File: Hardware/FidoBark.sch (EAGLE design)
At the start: 56 parts, among them Q1 MMBT2222A, T1 BPX81, U1 EDISON_CONNECTOR_FULLHEADER, U3 MCP73831, U4 TXB0108, U5 ADS1015, U6 PCA9306, U8 LSM9DS0

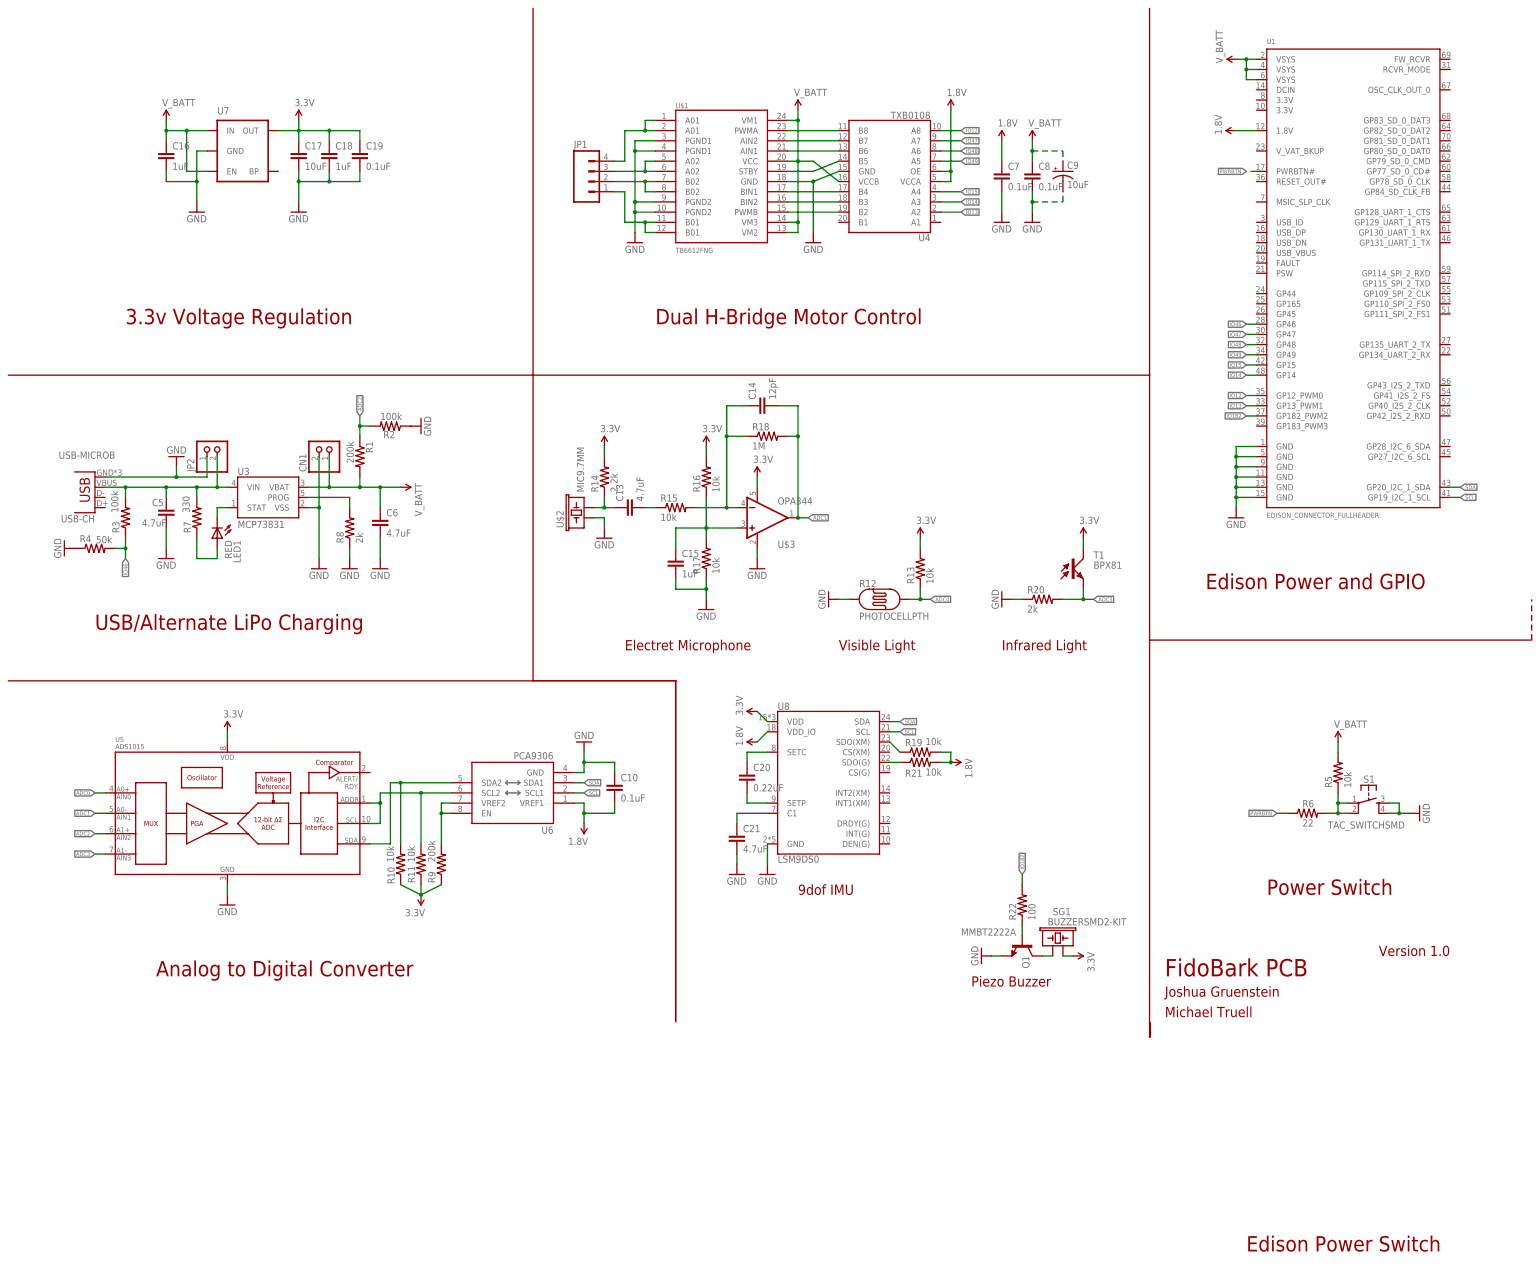
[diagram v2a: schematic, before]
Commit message: Cortex M4F based schematic start
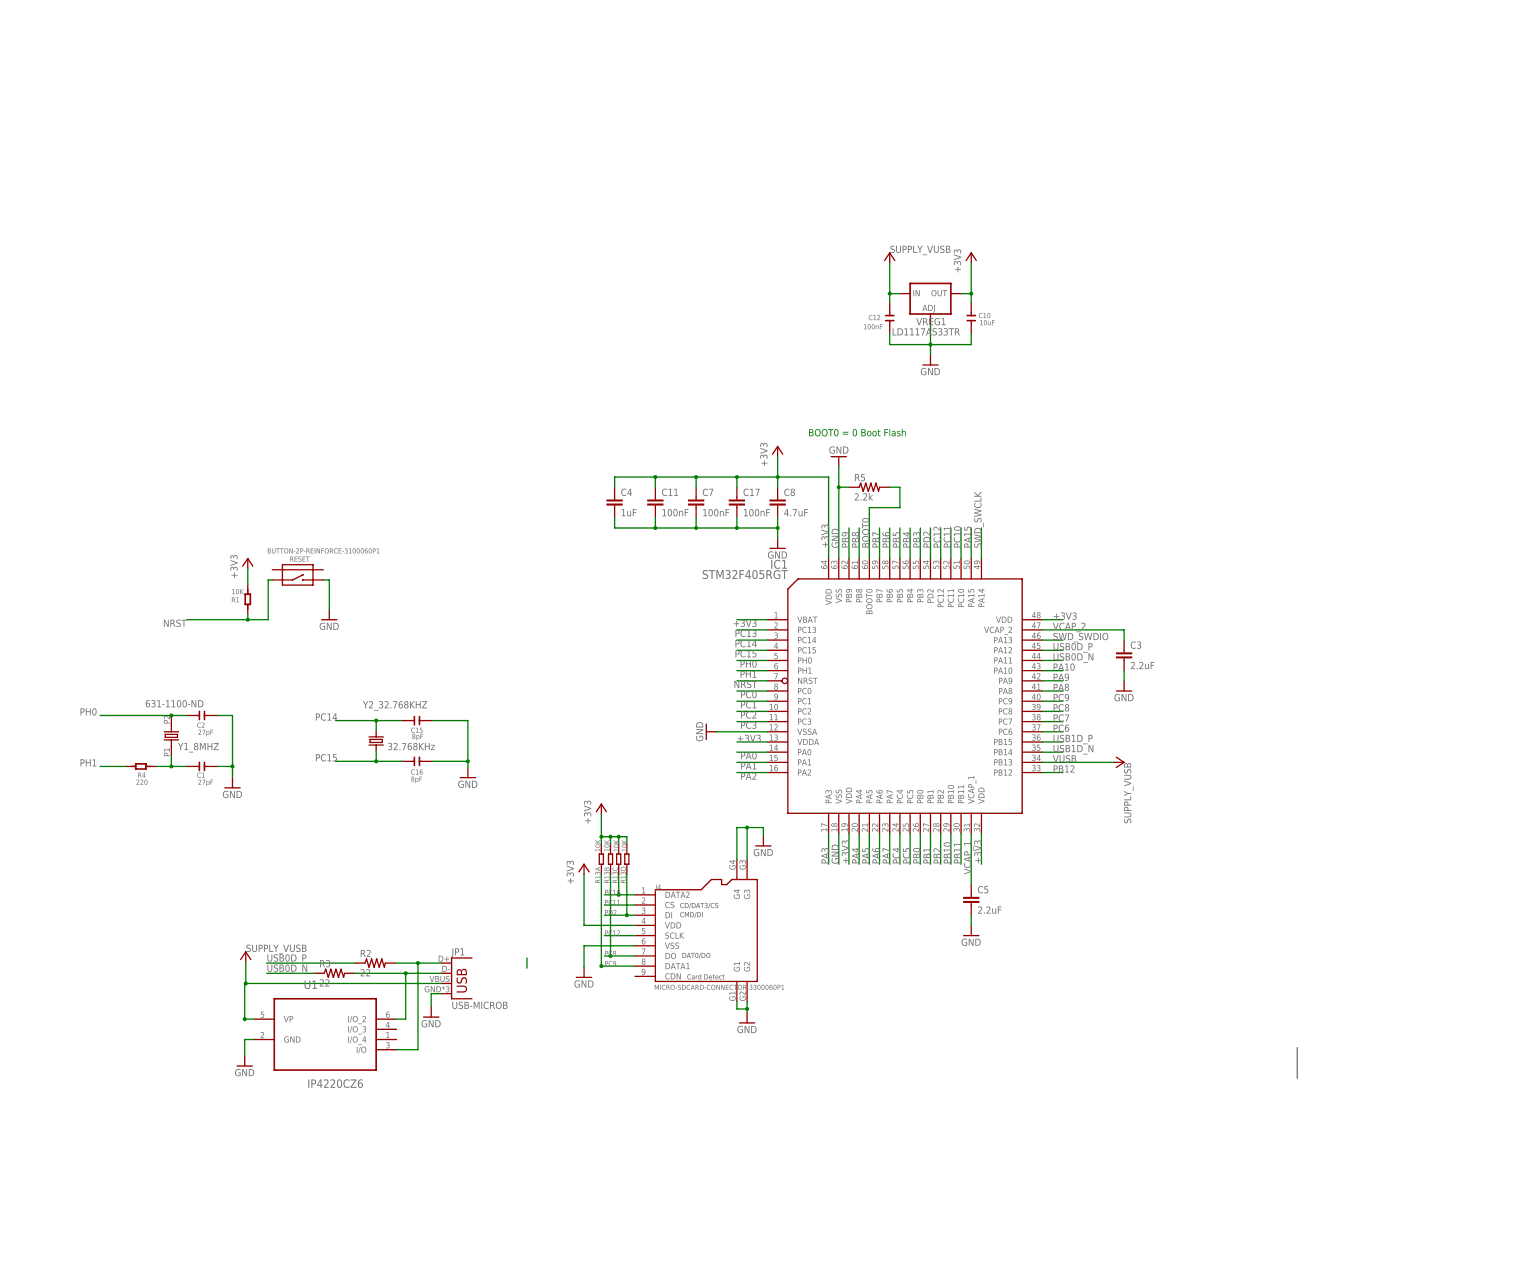
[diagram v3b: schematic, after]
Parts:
- removed C13, C21, C6: 4.7uF, SparkFun-Passives:CAP0603-CAP
- removed C14: 12pF, SparkFun-Passives:CAP0603-CAP
- removed C18: 1uF, SparkFun-Passives:CAP0603-CAP
- removed C19: 0.1uF, SparkFun-Passives:CAP0603-CAP
- removed C20: 0.22uF, SparkFun-Passives:CAP0603-CAP
- removed C9: 10uF, SparkFun-Capacitors:CAP_POL1206
- removed CN1: (no value), adafruit:JST_2PIN-SMT-RA
- removed JP2: (no value), pinhead:PINHD-1X2
- removed LED1: RED, adafruit:LEDCHIP-LED0603
- removed Q1: MMBT2222A, SparkFun-DiscreteSemi:TRANSISTOR_NPNMMBT2222A
- removed R10, R11, R15, R16, R17, R19, R21: 10k, adafruit:R-US_R0603
- removed R12: PHOTOCELLPTH, SparkFun-Sensors:PHOTOCELLPTH
- removed R14: 2.2k, adafruit:R-US_R0603
- removed R18: 1M, adafruit:R-US_R0603
- removed R20, R8: 2k, adafruit:R-US_R0603
- removed R22: 100, adafruit:R-US_R0603
- removed R6: 22, adafruit:R-US_R0603
- removed R7: 330, adafruit:R-US_R0603
- removed R9: 200k, adafruit:R-US_R0603
- removed S1: TAC_SWITCHSMD, SparkFun-Retired:TAC_SWITCHSMD
- removed SG1: BUZZERSMD2-KIT, SparkFun-Electromechanical:BUZZERSMD2-KIT
- removed T1: BPX81, opto-trans-siemens:BPX81
- removed U$1: TB6612FNG, SparkFun-PowerIC:TB6612FNG
- removed U$2: MIC9.7MM, SparkFun-Sensors:MIC9.7MM
- removed U$3: OPA344, SparkFun-AnalogIC:OPA344
- removed U3: MCP73831, SparkFun-PowerIC:MCP73831
- removed U4: TXB0108, SparkFun-DigitalIC:TXB0108
- removed U5: ADS1015, SparkFun-AnalogIC:ADS1015
- removed U6: PCA9306, SparkFun-DigitalIC:PCA9306
- removed U7: (no value), SparkFun-PowerIC:MIC52053.3V
- removed U8: LSM9DS0, SparkFun-DigitalIC:LSM9DS0
- removed USB-CH: USB-MICROB, SparkFun-Connectors:USB-MICROB
- added C1, C2: 27pF, OPL:C-0603
- added C11: 100nF, rcl:C-EUC0603
- added C12: 100nF, OPL:C-0603
- added C3: 2.2uF, rcl:C-EUC0603
- added C4: 1uF, rcl:C-EUC0603
- added IC1: STM32F405RGT, 0ben:STM32F405RGT
- added J4: MICRO-SDCARD-CONNECTOR-3300060P1, OPL:MICRO-SDCARD-CONNECTOR-3300060P1
- added RESET: BUTTON-2P-REINFORCE-3100060P1, OPL:BUTTON-2P-REINFORCE-3100060P1
- added VREG1: LD1117AS33TR, v-reg:LD117AS33TR
- added Y1_8MHZ: 631-1100-ND, dp_devices:OSC-XTAL-HC-49U-PTH
- added Y2_32.768KHZ: 32.768KHz, SparkFun:CRYSTALTC38H
- C10: value 0.1uF -> 10uF; device SparkFun-Passives:CAP0603-CAP -> OPL:C-0805
- C15, C16: value 1uF -> 8pF; device SparkFun-Passives:CAP0603-CAP -> OPL:C-0603
- C17: value 10uF -> 100nF; device SparkFun-Passives:CAP0603-CAP -> rcl:C-EUC0603
- C5: value 4.7uF -> 2.2uF; device SparkFun-Passives:CAP0603-CAP -> rcl:C-EUC0603
- C7: value 0.1uF -> 100nF; device SparkFun-Capacitors:CAP0603-CAP -> rcl:C-EUC0603
- C8: value 0.1uF -> 4.7uF; device SparkFun-Capacitors:CAP0603-CAP -> rcl:C-EUC0603
- JP1: value (none) -> USB-MICROB; device SparkFun-Connectors:M04PTH -> SparkFun-Connectors:USB-MICROB
- R1: value 200k -> 10K; device adafruit:R-US_R0603 -> OPL:R-0603; OPL_REF (none) -> 0010170P1 10K-5%-1/10W R0603
- R13: value 10k -> 10K; device adafruit:R-US_R0603 -> OPL:R-4R; OPL (none) -> 0040070P1 SMD RES ARRAY 10K OHM 4 RES 1206
- R2, R3: value 100k -> 22; device adafruit:R-US_R0603 -> rcl:R-US_R0603
- R4: value 50k -> 220; device adafruit:R-US_R0603 -> OPL:R-0603
- R5: value 10k -> 2.2k; device adafruit:R-US_R0603 -> rcl:R-US_R0603
- U1: value EDISON_CONNECTOR_FULLHEADER -> IP4220CZ6; device Edison:EDISON_CONNECTOR_FULLHEADER -> 0ben:IP4220CZ6
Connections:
- removed net 1.8V: C10.2, C7.1, R19.2, R21.2, U1.1.8V, U4.OE, U4.VCCA, U6.VREF1, U8.VDD_IO
- removed net 3.3V: C17.1, C18.1, C19.1, R10.1, R11.1, R13.2, R14.2, R16.2, R9.1, SG1.2, T1.C, U$3.V+, U5.VDD, U7.OUT, U8.VDD
- removed net ADC0: R12.P$2, R13.1, U5.AIN0
- removed net ADC1: C14.2, R18.2, U$3.OUT, U5.AIN1
- removed net ADC2: R1.1, R2.2, U5.AIN2
- removed net ADC3: R20.2, T1.E, U5.AIN3
- removed net IO12: U1.GP12_PWM0, U4.A8
- removed net IO13: U1.GP13_PWM1, U4.A2
- removed net IO14: U1.GP14, U4.A3
- removed net IO15: U1.GP15, U4.A4
- removed net IO182: R22.2, U1.GP182_PWM2
- removed net IO46: R3.1, R4.2, U1.GP46
- removed net IO47: U1.GP47, U4.A7
- removed net IO48: U1.GP48, U4.A6
- removed net IO49: U1.GP49, U4.A5
- removed net N$10: R8.2, U3.PROG
- removed net N$11: JP1.3, U$1.A02@5, U$1.A02@6
- removed net N$12: C5.1, JP2.2, R3.2, R7.2, U3.VIN, USB-CH.VBUS
- removed net N$13: JP1.2, U$1.B02@7, U$1.B02@8
- removed net N$14: R11.2, U5.ADDR, U5.SCL, U6.SCL2
- removed net N$15: U$1.PWMA, U4.B8
- removed net N$16: U$1.AIN2, U4.B7
- removed net N$17: JP1.1, U$1.B01@11, U$1.B01@12
- removed net N$18: JP1.4, U$1.A01@1, U$1.A01@2
- removed net N$19: U$1.AIN1, U4.B6
- removed net N$20: U$1.STBY, U4.B5
- removed net N$21: U$1.BIN1, U4.B4
- removed net N$22: U$1.BIN2, U4.B3
- removed net N$23: U$1.PWMB, U4.B2
- removed net N$24: R10.2, U5.SDA, U6.SDA2
- removed net N$25: R9.2, U6.EN, U6.VREF2
- removed net N$26: C20.1, U8.SETC
- removed net N$27: C20.2, U8.SETP
- removed net N$28: C13.1, R14.1, U$2.2
- removed net N$29: C13.2, R15.1
- removed net N$30: C14.1, R15.2, R18.1, U$3.-IN
- removed net N$31: C21.1, U8.C1
- removed net N$32: C15.1, R16.1, R17.2, U$3.+IN
- removed net N$33: R21.1, U8.SDO(G)
- removed net N$34: R19.1, U8.SDO(XM)
- removed net N$35: Q1.B, R22.1
- removed net N$36: Q1.C, SG1.1
- removed net N$7: R5.1, R6.2, S1.1, S1.2
- removed net N$8: LED1.A, R7.1
- removed net N$9: LED1.C, U3.STAT
- removed net PWRBTN: R6.1, U1.PWRBTN#
- removed net SCL: U1.GP19_I2C_1_SCL, U6.SCL1, U8.SCL
- removed net SDA: U1.GP20_I2C_1_SDA, U6.SDA1, U8.SDA
- removed net V_BATT: C16.1, C6.1, C8.1, C9.+, CN1.2, R1.2, R5.2, U$1.VCC, U$1.VM1, U$1.VM2, U$1.VM3, U1.VSYS@1, U1.VSYS@2, U1.VSYS@3, U3.VBAT, U4.VCCB, U7.EN, U7.IN
- new net +3V3: C10.1, C11.1, C17.1, C4.1, C7.1, C8.1, IC1.VBAT, IC1.VDD@19, IC1.VDD@32, IC1.VDD@48, IC1.VDD@64, IC1.VDDA, J4.VDD, R1.2, R13A.2, R13B.2, R13C.2, R13D.2, VREG1.OUT
- new net BOOT0: IC1.BOOT0, R5.2
- new net N$1: C1.1, R4.1, Y1_8MHZ.1
- new net NRST: IC1.NRST, R1.1, RESET.1
- new net PA0: IC1.PA0
- new net PA1: IC1.PA1
- new net PA10: IC1.PA10
- new net PA15: IC1.PA15
- new net PA2: IC1.PA2
- new net PA3: IC1.PA3
- new net PA4: IC1.PA4
- new net PA5: IC1.PA5
- new net PA6: IC1.PA6
- new net PA7: IC1.PA7
- new net PA8: IC1.PA8
- new net PA9: IC1.PA9
- new net PB0: IC1.PB0
- new net PB1: IC1.PB1
- new net PB10: IC1.PB10
- new net PB11: IC1.PB11
- new net PB12: IC1.PB12
- new net PB2: IC1.PB2
- new net PB3: IC1.PB3
- new net PB4: IC1.PB4
- new net PB5: IC1.PB5
- new net PB6: IC1.PB6
- new net PB7: IC1.PB7
- new net PB8: IC1.PB8
- new net PB9: IC1.PB9
- new net PC0: IC1.PC0
- new net PC1: IC1.PC1
- new net PC10: IC1.PC10, J4.DATA2, R13C.1
- new net PC11: IC1.PC11, J4.CS
- new net PC12: IC1.PC12, J4.SCLK
- new net PC13: IC1.PC13
- new net PC14: C15.1, IC1.PC14, Y2_32.768KHZ.2
- new net PC15: C16.1, IC1.PC15, Y2_32.768KHZ.1
- new net PC2: IC1.PC2
- new net PC3: IC1.PC3
- new net PC4: IC1.PC4
- new net PC5: IC1.PC5
- new net PC6: IC1.PC6
- new net PC7: IC1.PC7
- new net PC8: IC1.PC8, J4.DO, R13B.1
- new net PC9: IC1.PC9, J4.DATA1, R13A.1
- new net PD2: IC1.PD2, J4.DI, R13D.1
- new net PH0: C2.1, IC1.PH0, Y1_8MHZ.2
- new net PH1: IC1.PH1, R4.2
- new net SWD_SWCLK: IC1.PA14
- new net SWD_SWDIO: IC1.PA13
- new net USB0D_N: IC1.PA11, R3.1
- new net USB0D_P: IC1.PA12, R2.1
- new net USB0_D+: JP1.D+, R2.2, U1.I/O
- new net USB0_D-: JP1.D-, R3.2, U1.I/O_2
- new net USB1D_N: IC1.PB14
- new net USB1D_P: IC1.PB15
- new net VCAP_1: C5.1, IC1.VCAP_1
- new net VCAP_2: C3.1, IC1.VCAP_2
- new net VUSB: C12.1, IC1.PB13, JP1.VBUS, U1.VP, VREG1.IN
- net GND: now also C1.2, C10.2, C11.2, C12.2, C2.2, C3.2, C4.2, IC1.VSS@18, IC1.VSS@63, IC1.VSSA, J4.G1, J4.G2, J4.G3, J4.G4, J4.VSS, JP1.GND, R5.1, RESET.2, U1.GND, VREG1.ADJ; no longer C10.1, C18.2, C19.2, C21.2, C5.2, C6.2, C9.-, CN1.1, JP2.1, Q1.E, R12.P$1, R17.1, R2.1, R20.1, R4.1, R8.1, S1.3, S1.4, U$1.GND, U$1.PGND1@3, U$1.PGND1@4, U$1.PGND2@10, U$1.PGND2@9, U$2.1, U$3.V-, U1.GND@1, U1.GND@2, U1.GND@3, U1.GND@4, U1.GND@5, U1.GND@6, U3.VSS, U4.GND, U5.VSS, U6.GND, U7.GND, U8.GND, USB-CH.GND
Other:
- note added: "BOOT0 = 0 Boot Flash"
- note added: "CD/DAT3/CS"
- note added: "CMD/DI"
- note added: "Card Detect"
- note added: "DAT0/DO"
- note removed: "3.3v Voltage Regulation"
- note removed: "9dof IMU"
- note removed: "Analog to Digital Converter"
- note removed: "Dual H-Bridge Motor Control"
- note removed: "Edison Power Switch"
- note removed: "Edison Power and GPIO"
- note removed: "Electret Microphone"
- note removed: "FidoBark PCB"
- note removed: "Infrared Light"
- note removed: "Joshua Gruenstein"
- note removed: "Michael Truell"
- note removed: "Piezo Buzzer"
- note removed: "Power Switch"
- note removed: "USB/Alternate LiPo Charging"
- note removed: "Version 1.0"
- note removed: "Visible Light"
- moved on the sheet: C17, C5, C7, C8, R2, R3, R5
